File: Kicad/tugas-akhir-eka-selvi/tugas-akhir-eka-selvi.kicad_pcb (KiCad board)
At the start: 2 copper layers, 16.4 x 16.4 mm, 12 parts

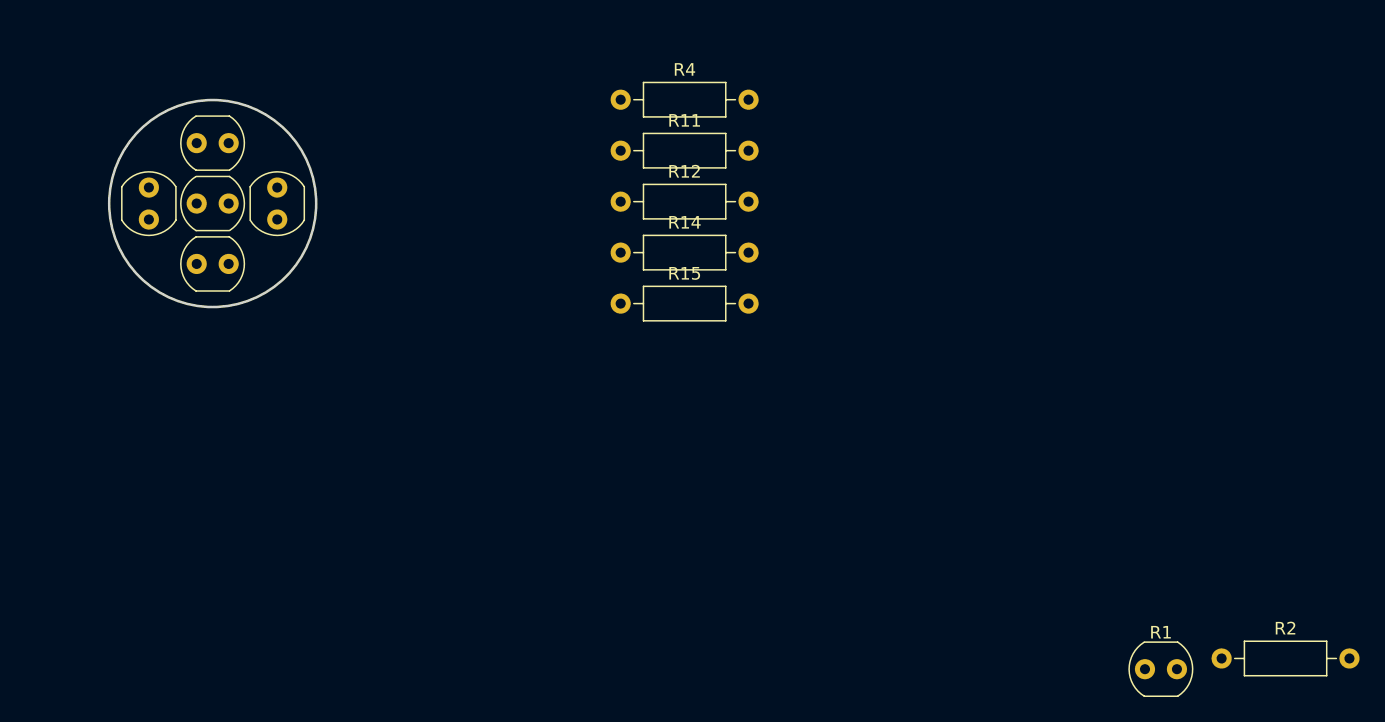
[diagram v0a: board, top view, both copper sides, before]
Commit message: Update array sensor schematic and PCB
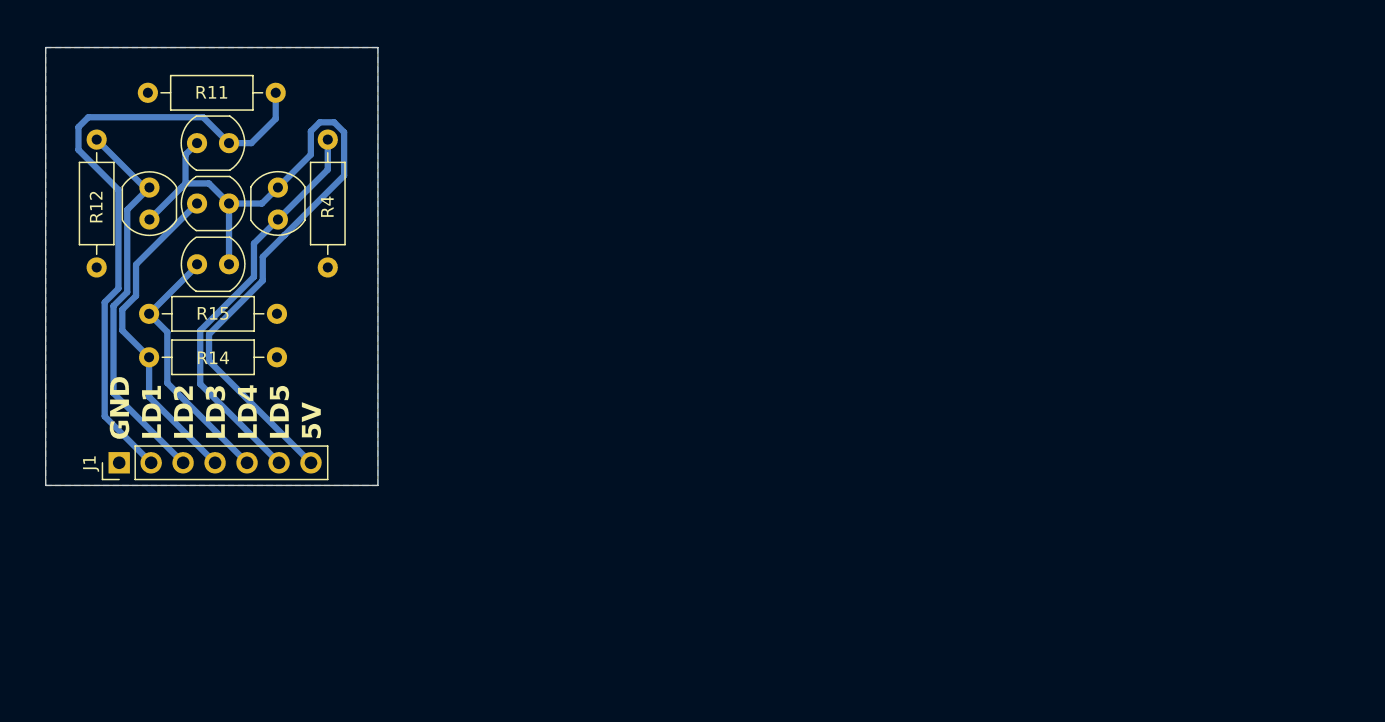
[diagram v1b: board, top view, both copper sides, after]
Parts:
- removed R1: LDR, OptoDevice:R_LDR_4.9x4.2mm_P2.54mm_Vertical
- removed R2: 10K, Resistor_THT:R_Axial_DIN0207_L6.3mm_D2.5mm_P10.16mm_Horizontal
- added J1: Conn_01x07, Connector_PinHeader_2.54mm:PinHeader_1x07_P2.54mm_Vertical, F.Cu at (140.0, 93.6)
- moved R12 41.9 mm to (138.3, 67.9), turned to -90 degrees
- moved R14 38.4 mm to (142.4, 85.2)
- moved R15 37.5 mm to (142.4, 81.8)
- moved R11 27.8 mm to (152.5, 64.2), turned to 180 degrees
- moved R4 23.5 mm to (156.6, 67.9), turned to -90 degrees
- moved R17 7.29 mm to (148.8, 77.8), turned to 180 degrees
- moved R5 6.58 mm to (152.7, 71.7), turned to -90 degrees
- moved R13 5.16 mm to (142.4, 74.3), turned to 90 degrees
- moved R16 4.04 mm to (148.8, 73.0), turned to 180 degrees
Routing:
- net +5V: track 0.00 -> 63.9 mm
- net /A0: track 0.00 -> 49.7 mm
- net /A4: track 0.00 -> 32.5 mm
- net /A1: track 0.00 -> 31.1 mm
- net /A2: track 0.00 -> 26.1 mm
- net /A3: track 0.00 -> 20.6 mm
- added copper zone on B.Cu, net GND
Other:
- board size 16.4 x 16.4 mm -> 26.4 x 34.8 mm
- board text added: "5V"
- board text added: "GND"
- board text added: "LD1"
- board text added: "LD2"
- board text added: "LD3"
- board text added: "LD4"
- board text added: "LD5"

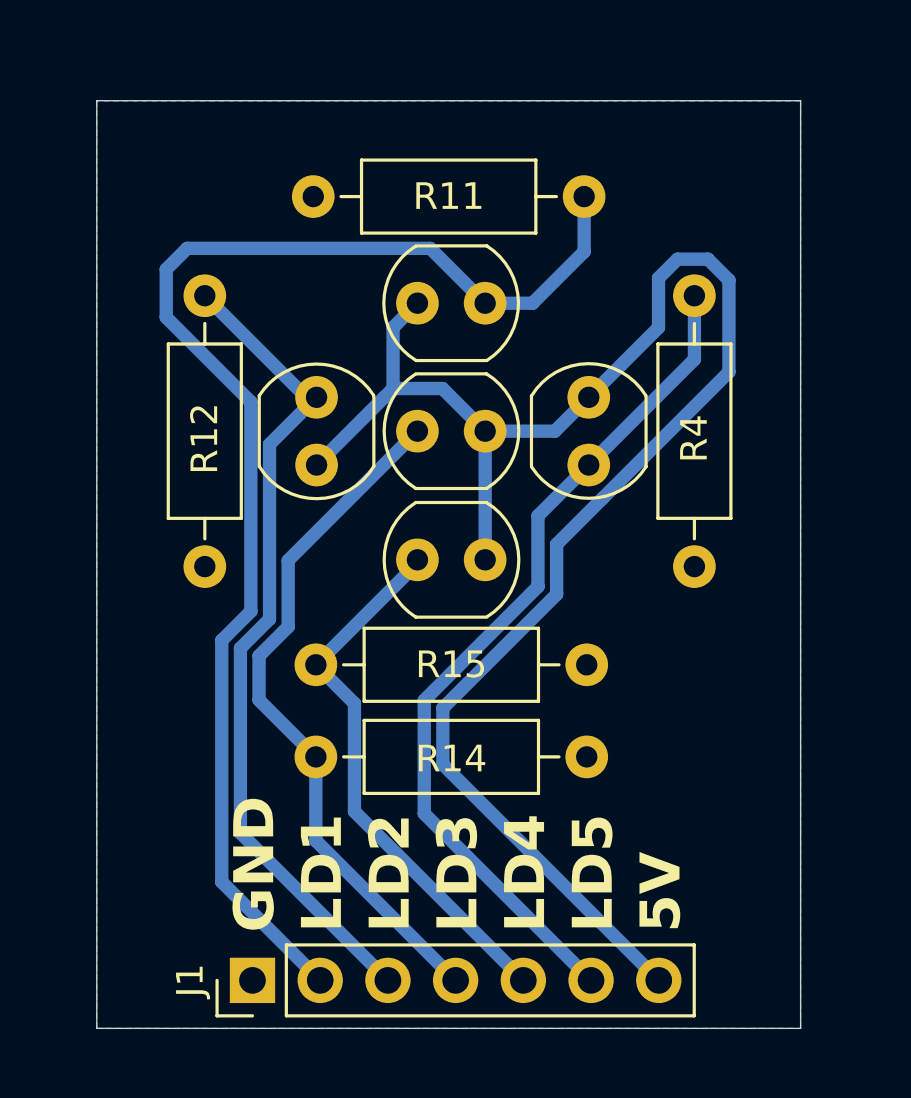
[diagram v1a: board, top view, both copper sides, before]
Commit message: Menambahkan Koding untuk membaca LDR dan di print ke serial monitor
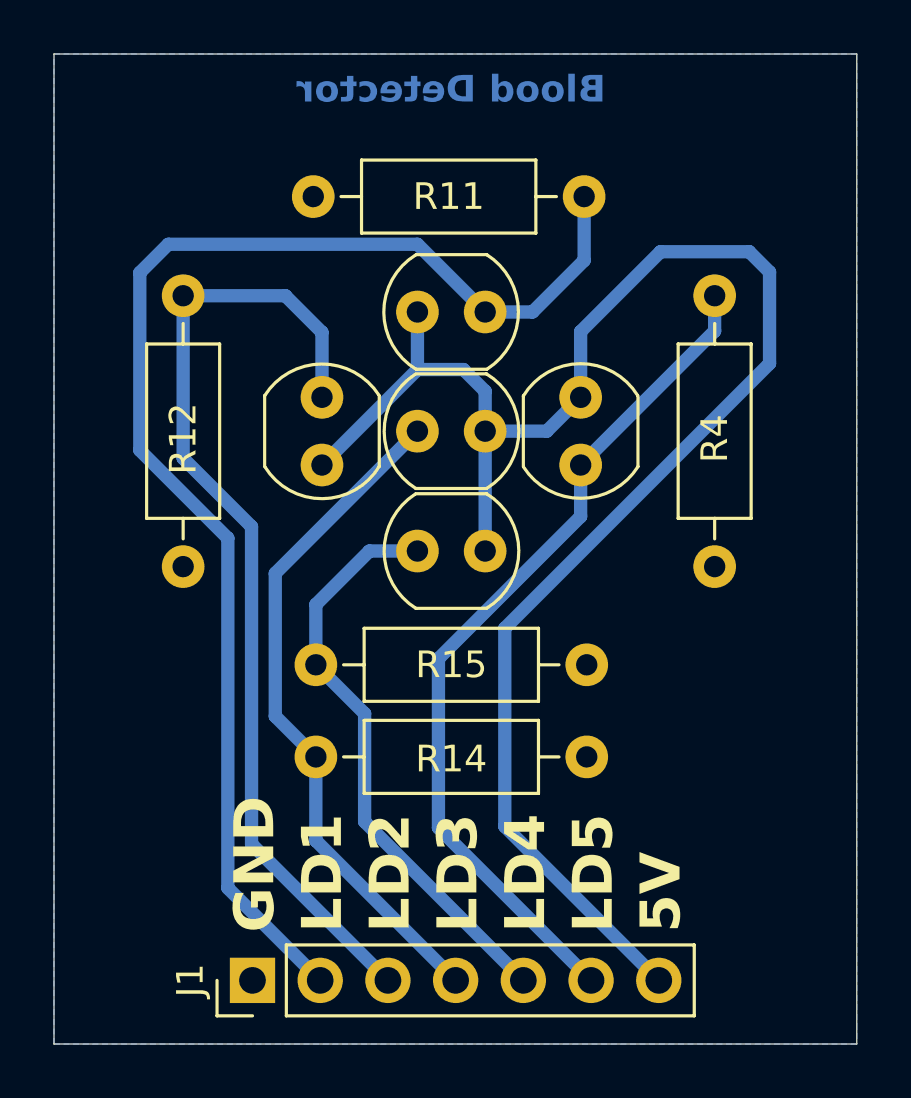
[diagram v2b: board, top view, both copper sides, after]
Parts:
- moved R12 0.81 mm to (137.4, 67.9)
- moved R4 0.76 mm to (157.4, 67.9)
- moved R17 0.33 mm to (148.8, 77.5)
- moved R3 0.33 mm to (146.2, 68.5)
- moved R5 0.30 mm to (152.3, 71.7)
- moved R13 0.20 mm to (142.6, 74.3)
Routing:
- net /A1: track 31.1 -> 37.1 mm
- net /A3: track 20.6 -> 22.0 mm
- net /A0: track 49.7 -> 50.7 mm
- net +5V: track 63.9 -> 64.4 mm
- net /A2: track 26.1 -> 25.6 mm
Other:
- board size 26.4 x 34.8 mm -> 30.1 x 37.1 mm
- board text added: "Blood Detector"
